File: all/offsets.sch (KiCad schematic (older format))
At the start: 7 parts, among them U1 TL072

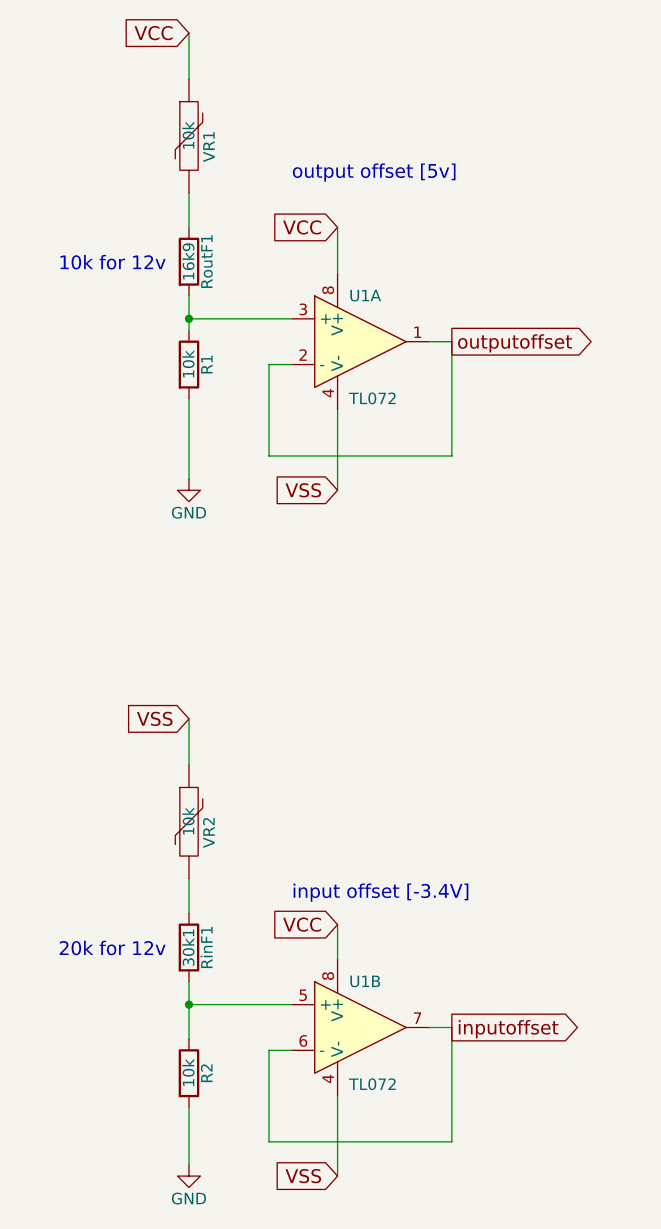
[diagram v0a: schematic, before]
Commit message: created an input only project, moved other to all
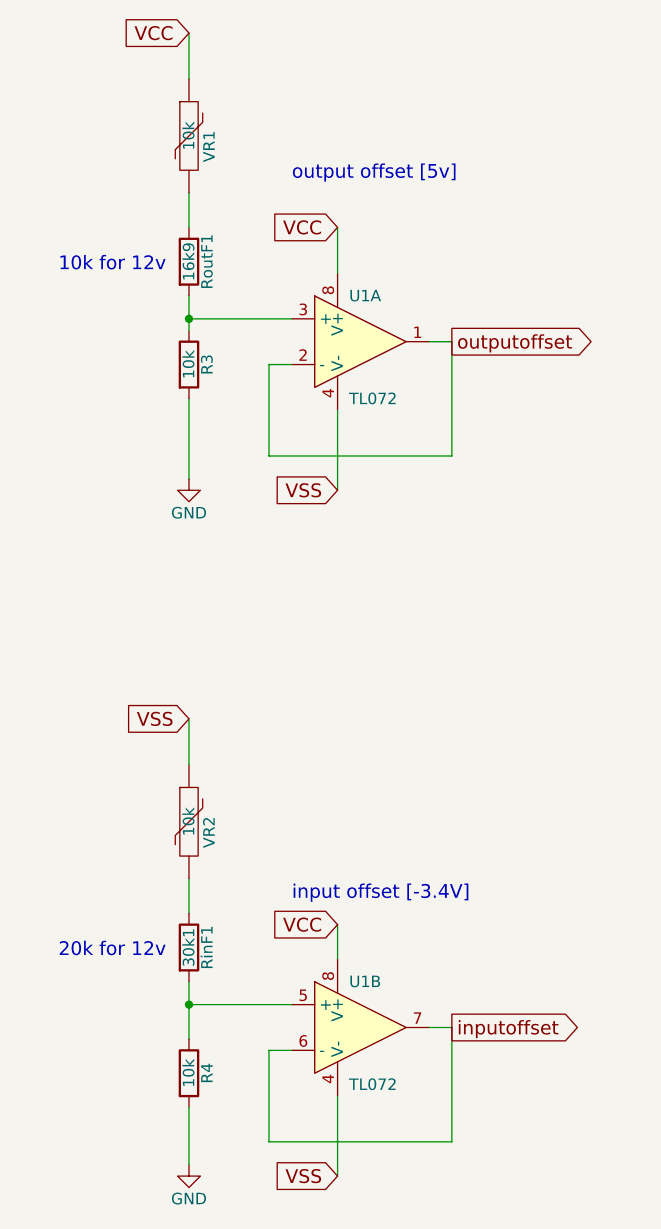
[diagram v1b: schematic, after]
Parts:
- renumbered R1 to R3, R2 to R4
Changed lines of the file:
@@
 LIBS:valves
 LIBS:bela-modular-cache
+LIBS:shift-cache
 EELAYER 25 0
 EELAYER END
@@
 	2150 2450 1700 2450
 $Comp
-L GND #PWR01
+L GND #PWR04
 U 1 1 58432FCD
 P 1700 6150
-F 0 "#PWR01" H 1700 5900 50  0001 C CNN
+F 0 "#PWR04" H 1700 5900 50  0001 C CNN
 F 1 "GND" H 1700 6000 50  0000 C CNN
 F 2 "" H 1700 6150 50  0000 C CNN
@@
 $EndComp
 $Comp
-L GND #PWR02
+L GND #PWR05
 U 1 1 58432FD3
 P 1700 3150
-F 0 "#PWR02" H 1700 2900 50  0001 C CNN
+F 0 "#PWR05" H 1700 2900 50  0001 C CNN
 F 1 "GND" H 1700 3000 50  0000 C CNN
 F 2 "" H 1700 3150 50  0000 C CNN
@@
 $EndComp
 $Comp
-L R R2
+L R R4
 U 1 1 58432FE0
 P 1700 5750
-F 0 "R2" V 1780 5750 50  0000 C CNN
+F 0 "R4" V 1780 5750 50  0000 C CNN
 F 1 "10k" V 1700 5750 50  0000 C CNN
 F 2 "" V 1630 5750 50  0000 C CNN
@@
 $EndComp
 $Comp
-L R R1
+L R R3
 U 1 1 58432FE7
 P 1700 2650
-F 0 "R1" V 1780 2650 50  0000 C CNN
+F 0 "R3" V 1780 2650 50  0000 C CNN
 F 1 "10k" V 1700 2650 50  0000 C CNN
 F 2 "" V 1630 2650 50  0000 C CNN
